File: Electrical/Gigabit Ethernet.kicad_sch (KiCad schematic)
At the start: 54 parts, among them IC1 RTL8125BG-CG, IC4 RTL8125BG-CG, J11 RJE3C1886401, J2 RJE3C1886401, Y1 25MHz, Y4 25MHz

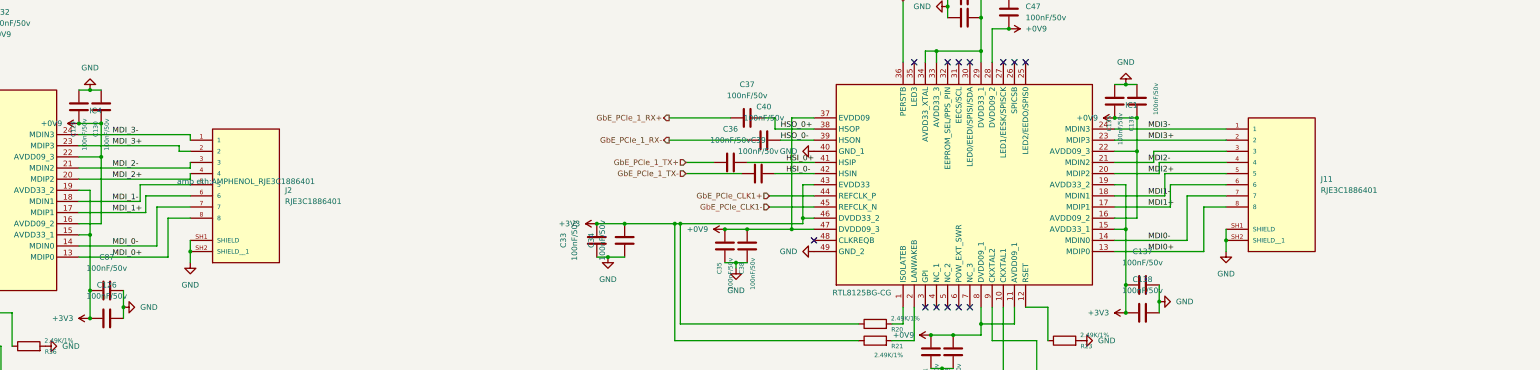
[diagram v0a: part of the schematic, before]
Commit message: changed ethernet port
changed to one that has built in magnetics
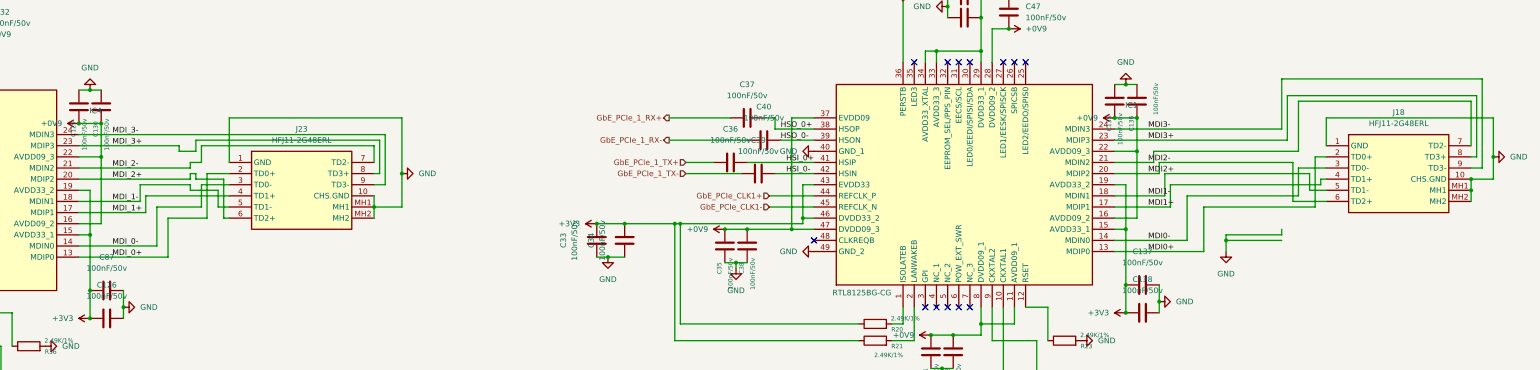
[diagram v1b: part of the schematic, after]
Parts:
- removed J11, J2: RJE3C1886401, amp eth:AMPHENOL_RJE3C1886401, symbol amp eth:RJE3C1886401
- added J18, J23: HFJ11-2G48ERL, new eth:HFJ112G48ERL, symbol new eth:HFJ11-2G48ERL
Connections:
- net GND: now also J18.1 (GND), J18.10 (CHS.GND), J18.MH1, J18.MH2, J23.1 (GND), J23.10 (CHS.GND), J23.MH1, J23.MH2
- net MDI0+: now also J18.2 (TD0+)
- net MDI0-: now also J18.3 (TD0-)
- net MDI1+: now also J18.4 (TD1+)
- net MDI1-: now also J18.5 (TD1-)
- net MDI2+: now also J18.6 (TD2+)
- net MDI2-: now also J18.7 (TD2-)
- net MDI3+: now also J18.8 (TD3+)
- net MDI3-: now also J18.9 (TD3-)
- net MDI_0+: now also J23.2 (TD0+)
- net MDI_0-: now also J23.3 (TD0-)
- net MDI_1+: now also J23.4 (TD1+)
- net MDI_1-: now also J23.5 (TD1-)
- net MDI_2+: now also J23.6 (TD2+)
- net MDI_2-: now also J23.7 (TD2-)
- net MDI_3+: now also J23.8 (TD3+)
- net MDI_3-: now also J23.9 (TD3-)

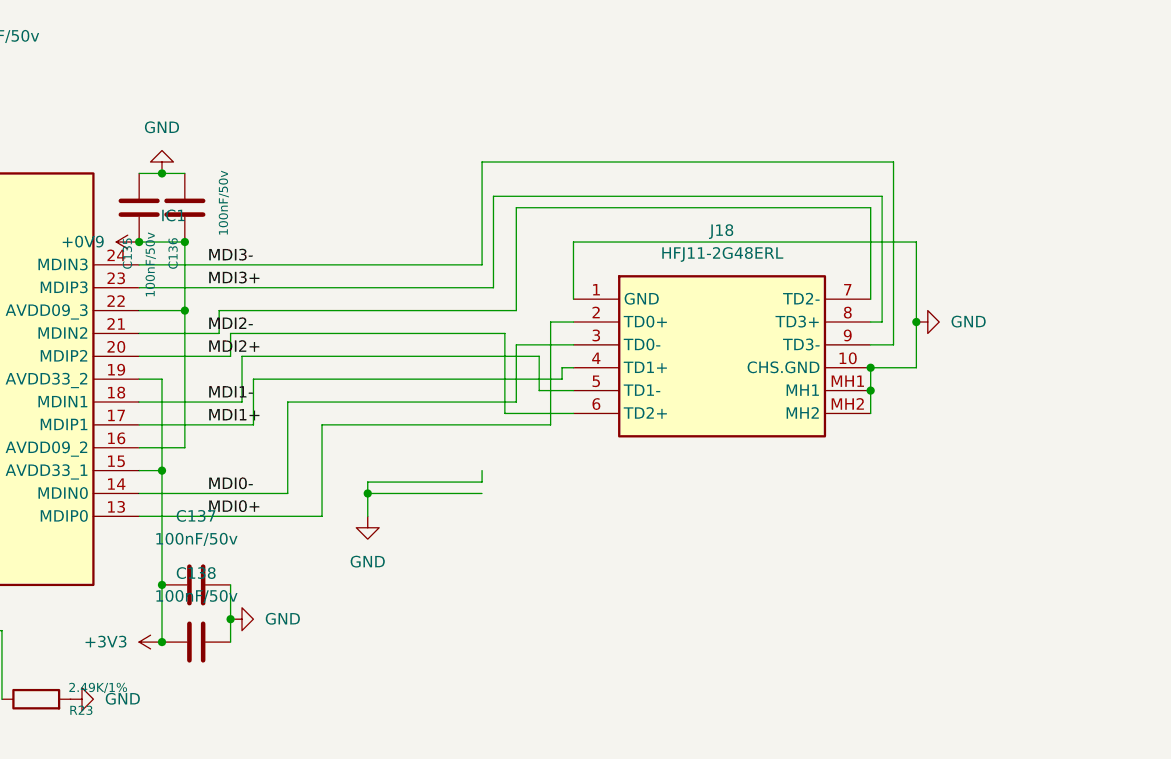
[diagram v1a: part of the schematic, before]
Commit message: further updates
split the ground plane for the sic437
use ethernet port that is available for purchase easily
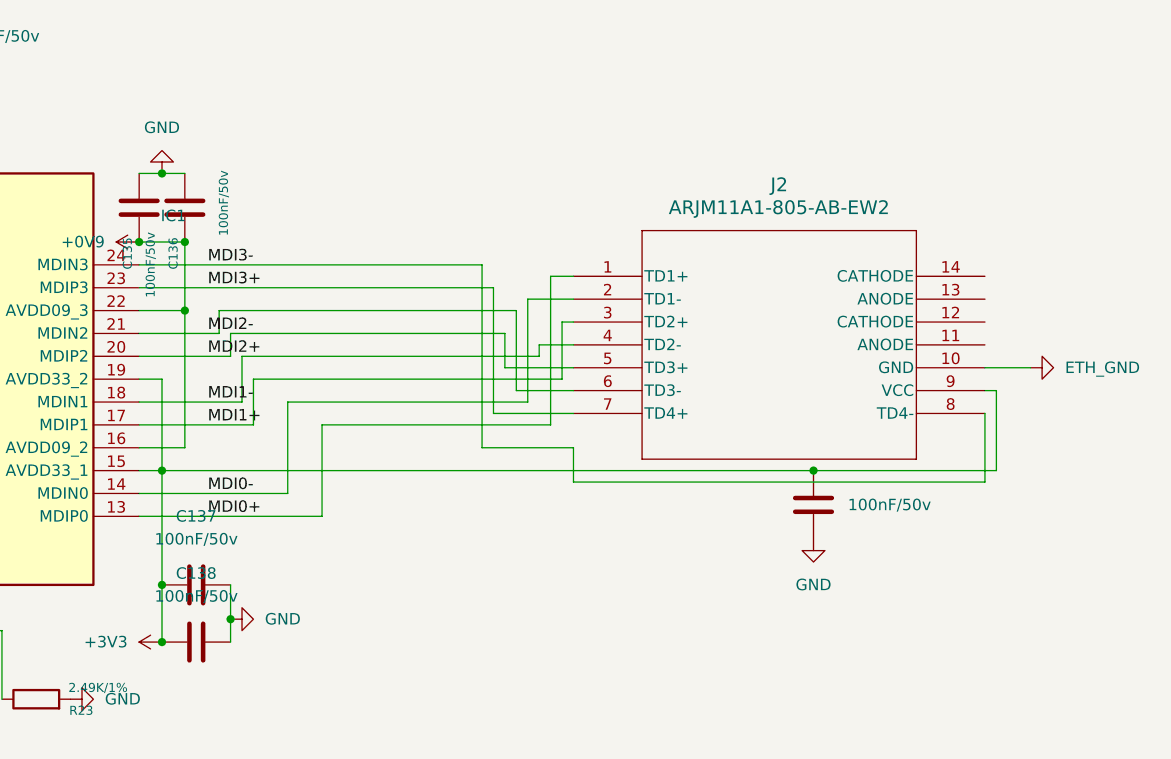
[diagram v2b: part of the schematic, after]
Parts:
- removed J18: HFJ11-2G48ERL, new eth:HFJ112G48ERL, symbol new eth:HFJ11-2G48ERL
- added C192: 100nF/50v, Capacitor_SMD:C_0402_1005Metric, symbol 100nf cap:C
- added J2: ARJM11A1-805-AB-EW2, mag eth:ARJM11A1-805-AB-EW2_ABR, symbol mag eth:ARJM11A1-805-AB-EW2
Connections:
- net +3V3: now also C192.2, J2.9 (VCC)
- net GND: now also C192.1
- net MDI0+: now also J2.1 (TD1+)
- net MDI0-: now also J2.2 (TD1-)
- net MDI1+: now also J2.3 (TD2+)
- net MDI1-: now also J2.4 (TD2-)
- net MDI2+: now also J2.5 (TD3+)
- net MDI2-: now also J2.6 (TD3-)
- net MDI3+: now also J2.7 (TD4+)
- net MDI3-: now also J2.8 (TD4-)
- new net ETH_GND: J2.10 (GND)

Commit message: further updates
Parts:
- removed J23: HFJ11-2G48ERL, new eth:HFJ112G48ERL, symbol new eth:HFJ11-2G48ERL
- added C193, C195, C196, C197, C198, C199: 2.2nF/2kv, Capacitor_SMD:C_1210_3225Metric_Pad1.33x2.70mm_HandSolder, symbol 100nf cap:C
- added C194: 100nF/50v, Capacitor_SMD:C_0402_1005Metric, symbol 100nf cap:C
- added J11: ARJM11A1-805-AB-EW2, mag eth:ARJM11A1-805-AB-EW2_ABR, symbol mag eth:ARJM11A1-805-AB-EW2
- added R102, R103, R104, R105: 1k/1%, Resistor_SMD:R_0603_1608Metric_Pad0.98x0.95mm_HandSolder, symbol Device:R
- added R25, R91: 1M/1%, Resistor_SMD:R_0603_1608Metric_Pad0.98x0.95mm_HandSolder, symbol Device:R
- C90, C91: value 12pF/50V -> 27pF/50V
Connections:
- net +3V3: now also C194.2, J11.9 (VCC), R102.1, R103.1, R104.1, R105.1
- net ETH_GND: now also C193.2, C196.2, C197.2, R91.2
- net GND: now also C193.1, C194.1, C195.1, C196.1, C197.1, C198.1, C199.1, R25.1, R91.1
- net MDI_0+: now also J11.1 (TD1+)
- net MDI_0-: now also J11.2 (TD1-)
- net MDI_1+: now also J11.3 (TD2+)
- net MDI_1-: now also J11.4 (TD2-)
- net MDI_2+: now also J11.5 (TD3+)
- net MDI_2-: now also J11.6 (TD3-)
- net MDI_3+: now also J11.7 (TD4+)
- net MDI_3-: now also J11.8 (TD4-)
- net at J2.11 (ANODE): now also R105.2
- net LED0_ETH1: now reaches J2.12 (CATHODE)
- net LED0_ETH1: now also IC1.30 (LED0/EEDI/SPISI/SDA)
- net at J2.13 (ANODE): now also R104.2
- net LED1_ETH1: now reaches J2.14 (CATHODE)
- net LED1_ETH1: now also IC1.27 (LED1/EESK/SPISCK)
- net LED1: now reaches IC4.27 (LED1/EESK/SPISCK)
- net LED1: now also J11.14 (CATHODE)
- net LED0: now reaches IC4.30 (LED0/EEDI/SPISI/SDA)
- net LED0: now also J11.12 (CATHODE)
- new net: J11.13 (ANODE), R103.2
- new net: J11.11 (ANODE), R102.2
- new net ETH_GND_2: C195.2, C198.2, C199.2, J11.10 (GND), R25.2
- no-connect marks 26 -> 22

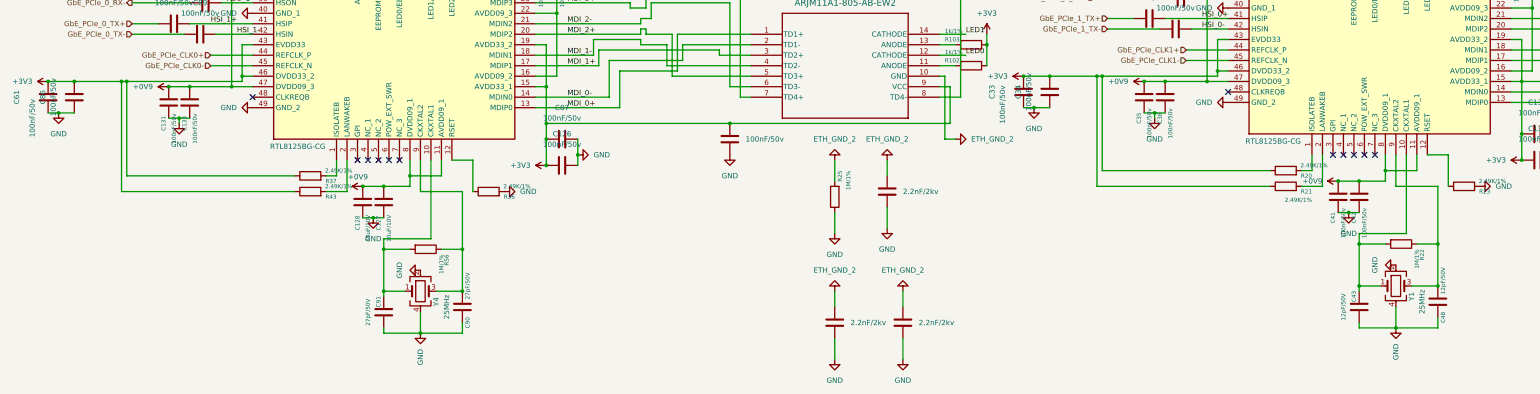
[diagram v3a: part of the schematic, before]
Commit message: add some fixes from initial prototype and fix 1v0 regulator
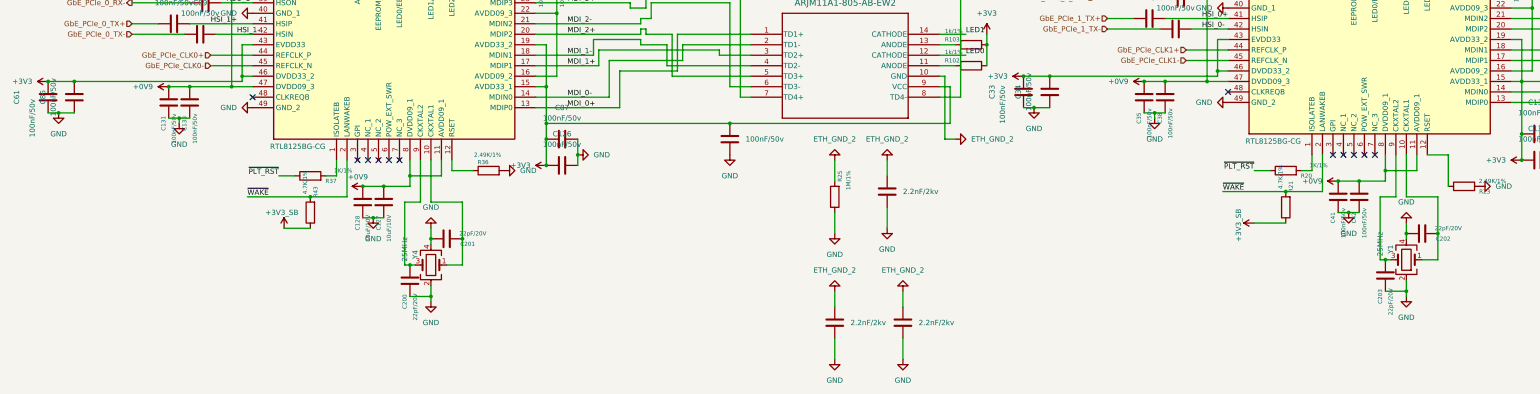
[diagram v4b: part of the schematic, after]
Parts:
- removed C43, C48: 12pF/50V, Capacitor_SMD:C_0402_1005Metric, symbol Device:C
- removed C90, C91: 27pF/50V, Capacitor_SMD:C_0402_1005Metric, symbol Device:C
- removed R22, R56: 1M/1%, Resistor_SMD:R_0402_1005Metric, symbol Device:R
- added C200, C201, C202, C203: 22pF/20V, Capacitor_SMD:C_0402_1005Metric, symbol Device:C
- R20, R37: value 2.49K/1% -> 1K/1%
- R21, R43: value 2.49K/1% -> 4.7K/1%
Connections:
- net +3V3: no longer R20.1, R21.1, R37.1, R43.1
- net GND: now also C200.1, C201.2, C202.2, C203.1
- net ~{PLT_RST}: now also R20.1, R37.1
- net at IC4.9 (CKXTAL2), Y4.3: now also C200.2
- net ~{WAKE}: now reaches IC1.2 (LANWAKEB), R21.2
- net ~{WAKE}: now also IC4.2 (LANWAKEB), R43.2
- net at IC1.10 (CKXTAL1), Y1.1: now also C202.1
- net at IC1.9 (CKXTAL2), Y1.3: now also C203.2
- net at IC4.10 (CKXTAL1), Y4.1: now also C201.1
- new net +3V3_SB: R21.1, R43.1
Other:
- moved on the sheet: R36, R43, Y4
